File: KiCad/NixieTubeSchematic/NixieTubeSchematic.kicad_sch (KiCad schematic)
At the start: 26 parts

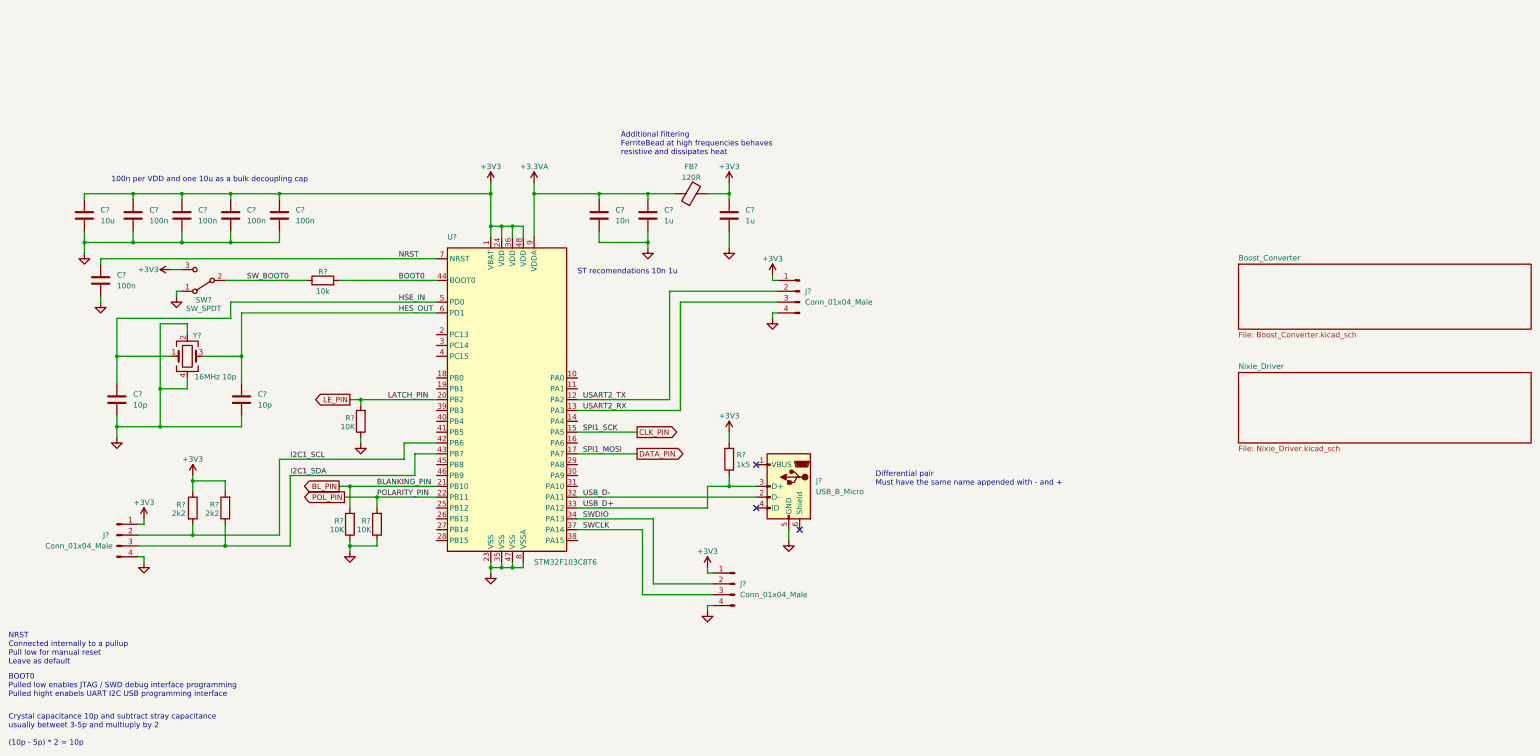
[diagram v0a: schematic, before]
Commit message: Schematic for DS3231 RTC and AT24C32 EEPROM added
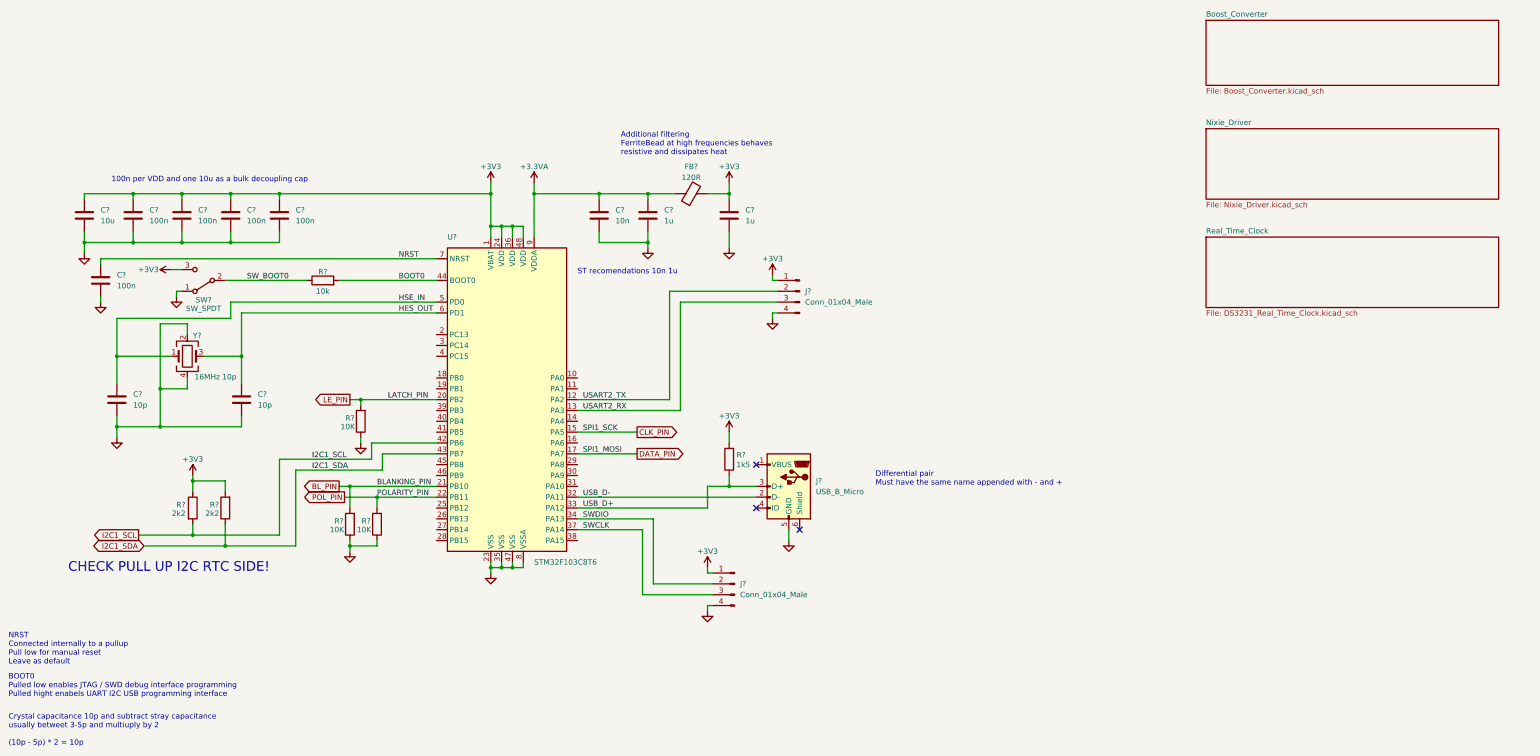
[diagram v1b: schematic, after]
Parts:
- removed J?: Conn_01x04_Male, symbol Connector:Conn_01x04_Male
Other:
- added sheet Real_Time_Clock (DS3231_Real_Time_Clock.kicad_sch)
- note added: "CHECK PULL UP I2C RTC SIDE!"

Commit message: Small changes
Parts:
- removed 10K: R?, symbol Device:R
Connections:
- net BL_PIN renamed BL_PIN_LV
- net CLK_PIN renamed CLK_PIN_LV
- net DATA_PIN renamed DATA_PIN_LV
- net LE_PIN renamed LE_PIN_LV
- net POL_PIN: no longer names the net of U?.22 (PB11)
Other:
- added sheet Level_Shift_Converter (Level_Shift_Converter_STM32_HV5530.kicad_sch)
- note added: "CHECK PULL UP I2C RTC SIDE! Goode idea to keep them on HOAST side"
- note removed: "CHECK PULL UP I2C RTC SIDE!"
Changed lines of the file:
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@@
   (junction (at 196.85 110.49) (diameter 0) (color 0 0 0 0)
   )
-  (junction (at 114.3 113.03) (diameter 0) (color 0 0 0 0)
-  )
   (junction (at 110.49 90.17) (diameter 0) (color 0 0 0 0)
   )
@@
   )
   (junction (at 78.74 124.46) (diameter 0) (color 0 0 0 0)
-  )
-  (junction (at 107.95 124.46) (diameter 0) (color 0 0 0 0)
   )
   (junction (at 80.01 41.91) (diameter 0) (color 0 0 0 0)
@@
   (no_connect (at 203.2 105.41))
   (no_connect (at 213.36 120.65))
-  (wire (pts (xy 107.95 124.46) (xy 107.95 125.73))
+  (wire (pts (xy 107.95 123.19) (xy 107.95 125.73))
     (stroke (width 0) (type default))
   )
@@
     (stroke (width 0) (type default))
   )
-  (wire (pts (xy 91.44 104.14) (xy 91.44 121.92))
+  (wire (pts (xy 83.82 104.14) (xy 83.82 121.92))
     (stroke (width 0) (type default))
   )
@@
     (stroke (width 0) (type default))
   )
-  (wire (pts (xy 106.68 113.03) (xy 114.3 113.03))
-    (stroke (width 0) (type default))
-  )
   (wire (pts (xy 113.03 104.14) (xy 113.03 100.33))
     (stroke (width 0) (type default))
@@
     (stroke (width 0) (type default))
   )
-  (wire (pts (xy 95.25 106.68) (xy 115.57 106.68))
+  (wire (pts (xy 87.63 106.68) (xy 115.57 106.68))
     (stroke (width 0) (type default))
   )
@@
     (stroke (width 0) (type default))
   )
-  (wire (pts (xy 78.74 124.46) (xy 95.25 124.46))
+  (wire (pts (xy 78.74 124.46) (xy 87.63 124.46))
     (stroke (width 0) (type default))
   )
@@
     (stroke (width 0) (type default))
   )
-  (wire (pts (xy 91.44 104.14) (xy 113.03 104.14))
+  (wire (pts (xy 83.82 104.14) (xy 113.03 104.14))
     (stroke (width 0) (type default))
   )
@@
     (stroke (width 0) (type default))
   )
-  (wire (pts (xy 107.95 123.19) (xy 107.95 124.46))
-    (stroke (width 0) (type default))
-  )
   (wire (pts (xy 161.29 90.17) (xy 182.88 90.17))
     (stroke (width 0) (type default))
@@
     (stroke (width 0) (type default))
   )
-  (wire (pts (xy 114.3 113.03) (xy 128.27 113.03))
-    (stroke (width 0) (type default))
-  )
   (wire (pts (xy 210.82 120.65) (xy 210.82 123.19))
     (stroke (width 0) (type default))
@@
     (stroke (width 0) (type default))
   )
-  (wire (pts (xy 91.44 121.92) (xy 71.12 121.92))
+  (wire (pts (xy 83.82 121.92) (xy 71.12 121.92))
     (stroke (width 0) (type default))
   )
@@
     (stroke (width 0) (type default))
   )
-  (wire (pts (xy 114.3 124.46) (xy 107.95 124.46))
-    (stroke (width 0) (type default))
-  )
   (wire (pts (xy 107.95 90.17) (xy 110.49 90.17))
     (stroke (width 0) (type default))
@@
     (stroke (width 0) (type default))
   )
-  (wire (pts (xy 114.3 113.03) (xy 114.3 115.57))
-    (stroke (width 0) (type default))
-  )
   (wire (pts (xy 146.05 49.53) (xy 146.05 52.07))
     (stroke (width 0) (type default))
@@
     (stroke (width 0) (type default))
   )
-  (wire (pts (xy 95.25 124.46) (xy 95.25 106.68))
+  (wire (pts (xy 87.63 124.46) (xy 87.63 106.68))
     (stroke (width 0) (type default))
   )
@@
   )
   (wire (pts (xy 68.58 50.8) (xy 68.58 53.34))
-    (stroke (width 0) (type default))
-  )
-  (wire (pts (xy 114.3 123.19) (xy 114.3 124.46))
     (stroke (width 0) (type default))
   )
@@
     (effects (font (size 1.27 1.27)) (justify left bottom))
   )
-  (text "CHECK PULL UP I2C RTC SIDE!" (at 41.91 130.81 0)
+  (text "CHECK PULL UP I2C RTC SIDE!\n\nGoode idea to keep them on HOAST side"
+    (at 30.48 138.43 0)
     (effects (font (size 2.27 2.27)) (justify left bottom))
   )
@@
     (effects (font (size 1.27 1.27)) (justify left bottom))
   )
-  (label "POLARITY_PIN" (at 114.3 113.03 0) (fields_autoplaced)
-    (effects (font (size 1.27 1.27)) (justify left bottom))
-  )
   (label "SWDIO" (at 162.56 118.11 0) (fields_autoplaced)
     (effects (font (size 1.27 1.27)) (justify left bottom))
@@
     (effects (font (size 1.27 1.27)) (justify left bottom))
   )
-  (global_label "POL_PIN" (shape output) (at 106.68 113.03 180) (fields_autoplaced)
+  (global_label "LE_PIN_LV" (shape output) (at 107.95 90.17 180) (fields_autoplaced)
     (effects (font (size 1.27 1.27)) (justify right))
-    (property "Intersheetrefs" "${INTERSHEET_REFS}" (at 96.4655 112.9506 0)
+    (property "Intersheetrefs" "${INTERSHEET_REFS}" (at 95.6099 90.17 0)
       (effects (font (size 1.27 1.27)) (justify right) hide)
-    )
-  )
-  (global_label "CLK_PIN" (shape output) (at 175.26 97.79 0) (fields_autoplaced)
-    (effects (font (size 1.27 1.27)) (justify left))
-    (property "Intersheetrefs" "${INTERSHEET_REFS}" (at 185.4141 97.7106 0)
-      (effects (font (size 1.27 1.27)) (justify left) hide)
     )
   )
@@
     )
   )
-  (global_label "BL_PIN" (shape output) (at 105.41 110.49 180) (fields_autoplaced)
+  (global_label "DATA_PIN_LV" (shape output) (at 175.26 102.87 0) (fields_autoplaced)
+    (effects (font (size 1.27 1.27)) (justify left))
+    (property "Intersheetrefs" "${INTERSHEET_REFS}" (at 189.8378 102.87 0)
+      (effects (font (size 1.27 1.27)) (justify left) hide)
+    )
+  )
+  (global_label "CLK_PIN_LV" (shape output) (at 175.26 97.79 0) (fields_autoplaced)
+    (effects (font (size 1.27 1.27)) (justify left))
+    (property "Intersheetrefs" "${INTERSHEET_REFS}" (at 188.9911 97.79 0)
+      (effects (font (size 1.27 1.27)) (justify left) hide)
+    )
+  )
+  (global_label "BL_PIN_LV" (shape output) (at 105.41 110.49 180) (fields_autoplaced)
     (effects (font (size 1.27 1.27)) (justify right))
-    (property "Intersheetrefs" "${INTERSHEET_REFS}" (at 96.5259 110.4106 0)
-      (effects (font (size 1.27 1.27)) (justify right) hide)
-    )
-  )
-  (global_label "DATA_PIN" (shape output) (at 175.26 102.87 0) (fields_autoplaced)
-    (effects (font (size 1.27 1.27)) (justify left))
-    (property "Intersheetrefs" "${INTERSHEET_REFS}" (at 186.2607 102.7906 0)
-      (effects (font (size 1.27 1.27)) (justify left) hide)
-    )
-  )
-  (global_label "LE_PIN" (shape output) (at 107.95 90.17 180) (fields_autoplaced)
-    (effects (font (size 1.27 1.27)) (justify right))
-    (property "Intersheetrefs" "${INTERSHEET_REFS}" (at 99.1869 90.0906 0)
+    (property "Intersheetrefs" "${INTERSHEET_REFS}" (at 92.9489 110.49 0)
       (effects (font (size 1.27 1.27)) (justify right) hide)
     )
@@
     )
   )
-  (symbol (lib_id "Device:R") (at 114.3 119.38 180) (unit 1)
-    (in_bom yes) (on_board yes) (dnp no)
-    (property "Reference" "10K" (at 111.252 120.65 0)
-      (effects (font (size 1.27 1.27)))
-    )
-    (property "Value" "R?" (at 111.76 118.618 0)
-      (effects (font (size 1.27 1.27)))
-    )
-    (property "Footprint" "" (at 116.078 119.38 90)
-      (effects (font (size 1.27 1.27)) hide)
-    )
-    (property "Datasheet" "~" (at 114.3 119.38 0)
-      (effects (font (size 1.27 1.27)) hide)
-    )
-    (pin "1")
-    (pin "2")
-    (instances
-      (project "NixieTubeSchematic"
-        (path "/15bbe1f7-5063-4eec-b8be-2e4a42a15139"
-          (reference "10K") (unit 1)
-        )
-      )
-    )
-  )
   (symbol (lib_id "power:GND") (at 210.82 123.19 0) (unit 1)
     (in_bom yes) (on_board yes) (dnp no) (fields_autoplaced)
@@
       )
     )
+  )
+  (sheet (at 308.61 77.47) (size 68.58 16.51) (fields_autoplaced)
+    (stroke (width 0.1524) (type solid))
+    (fill (color 0 0 0 0.0000))
+    (property "Sheetname" "Level_Shift_Converter" (at 308.61 76.7584 0)
+      (effects (font (size 1.27 1.27)) (justify left bottom))
+    )
+    (property "Sheetfile" "Level_Shift_Converter_STM32_HV5530.kicad_sch" (at 308.61 94.5646 0)
+      (effects (font (size 1.27 1.27)) (justify left top))
+    )
+    (property "Field2" "" (at 308.61 77.47 0)
+      (effects (font (size 1.27 1.27)) hide)
+    )
+    (instances
+      (project "NixieTubeSchematic"
+        (path "/15bbe1f7-5063-4eec-b8be-2e4a42a15139" (page "5"))
+      )
+    )
